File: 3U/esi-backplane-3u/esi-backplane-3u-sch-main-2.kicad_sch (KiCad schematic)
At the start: 16 parts

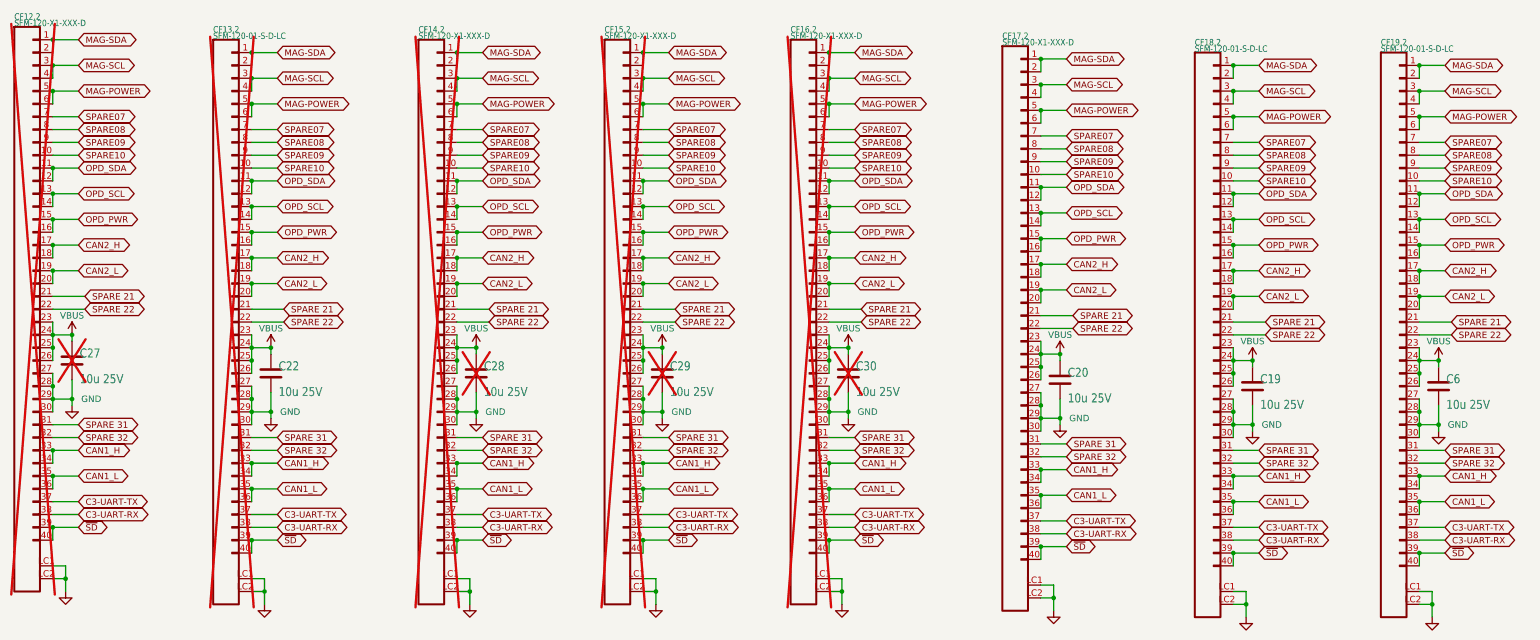
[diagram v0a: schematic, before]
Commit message: Moved RW and mag cards back, changes spare tracing side -- updated DNP w changes
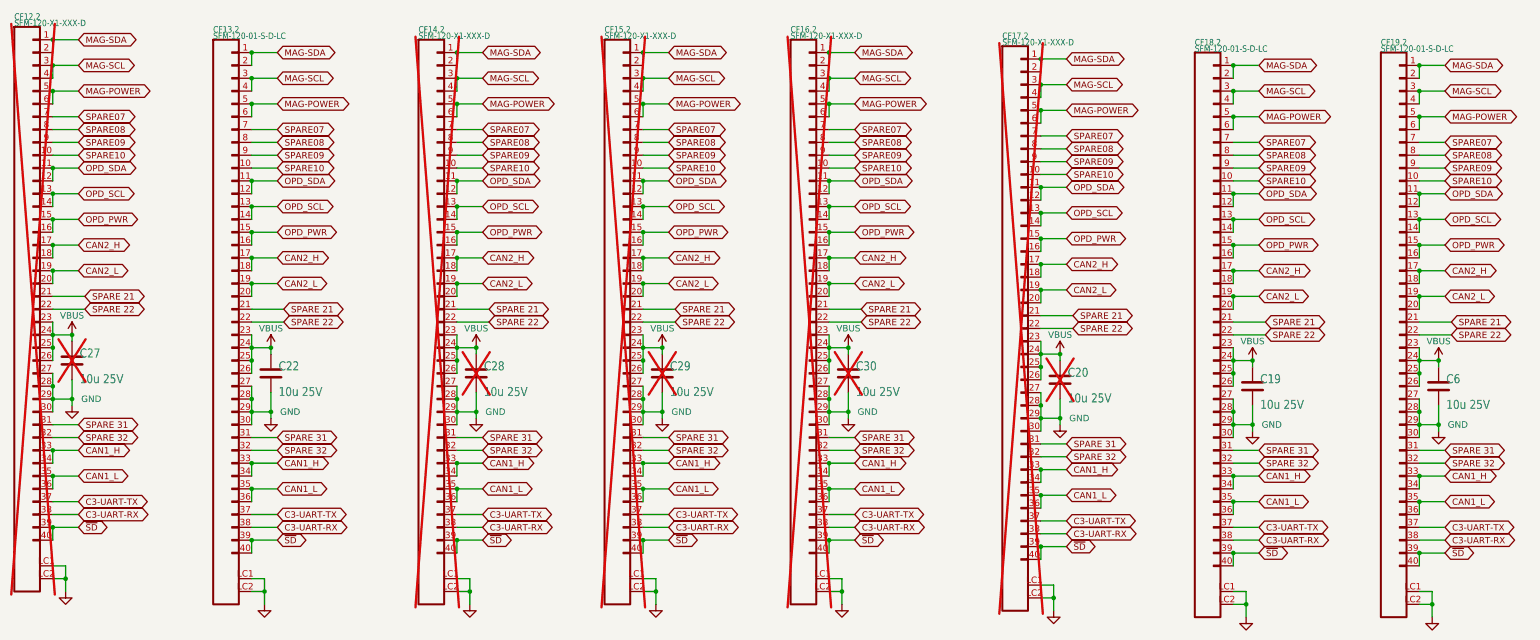
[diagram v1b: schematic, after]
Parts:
- C20, CF17.2: now not fitted
- CF13.2: now fitted
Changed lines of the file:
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@@
 		(in_bom yes)
 		(on_board yes)
-		(dnp no)
+		(dnp yes)
 		(property "Reference" "CF17.2"
 			(at 271.78 73.66 0)
@@
 		(in_bom yes)
 		(on_board yes)
-		(dnp yes)
+		(dnp no)
 		(property "Reference" "CF13.2"
 			(at 115.57 72.39 0)
@@
 		(in_bom yes)
 		(on_board yes)
-		(dnp no)
+		(dnp yes)
 		(property "Reference" "C20"
 			(at 284.734 140.589 0)

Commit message: Board switches and microstrip mask change
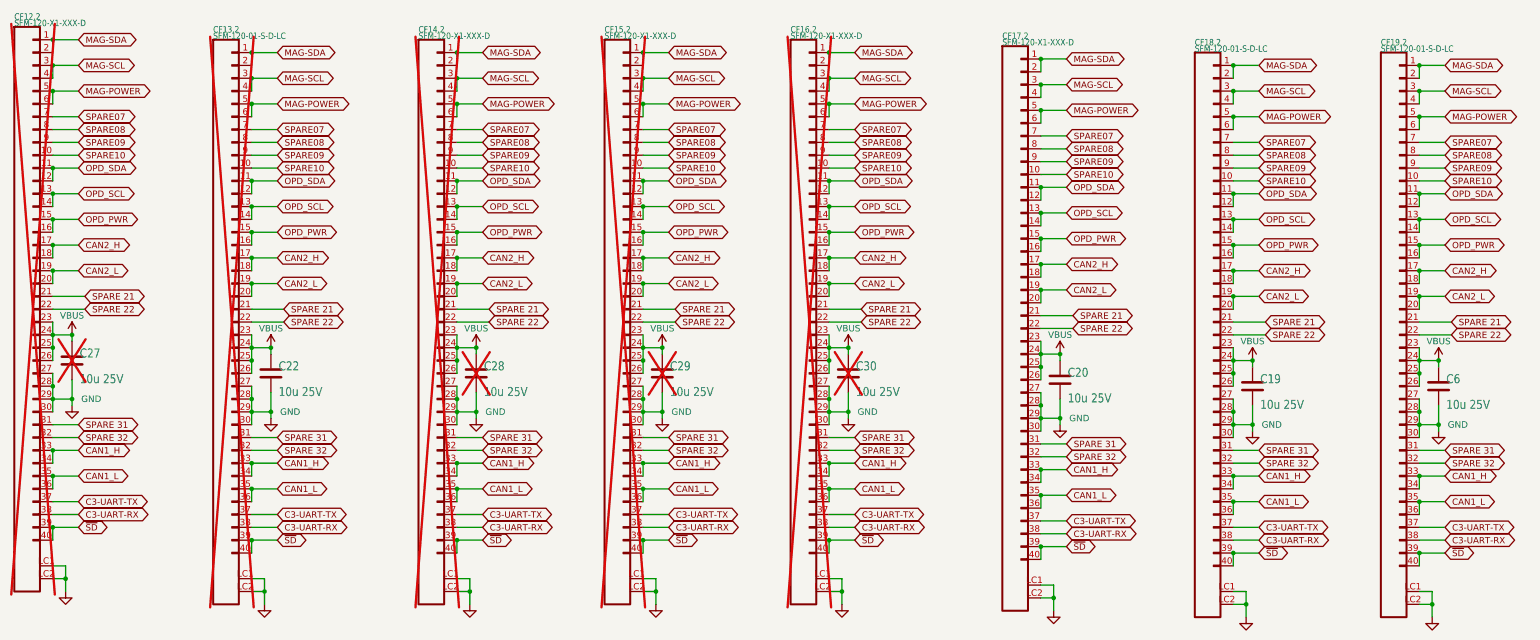
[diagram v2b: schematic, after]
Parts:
- C20, CF17.2: now fitted
- CF13.2: now not fitted
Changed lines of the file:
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@@
 		(in_bom yes)
 		(on_board yes)
-		(dnp yes)
+		(dnp no)
 		(property "Reference" "CF17.2"
 			(at 271.78 73.66 0)
@@
 		(in_bom yes)
 		(on_board yes)
-		(dnp no)
+		(dnp yes)
 		(property "Reference" "CF13.2"
 			(at 115.57 72.39 0)
@@
 		(in_bom yes)
 		(on_board yes)
-		(dnp yes)
+		(dnp no)
 		(property "Reference" "C20"
 			(at 284.734 140.589 0)
